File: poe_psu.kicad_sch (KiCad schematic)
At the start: 41 parts, among them T1 HR051142, U2 SI3404-A-GM, U3 EL3H7-G, U4 AN431

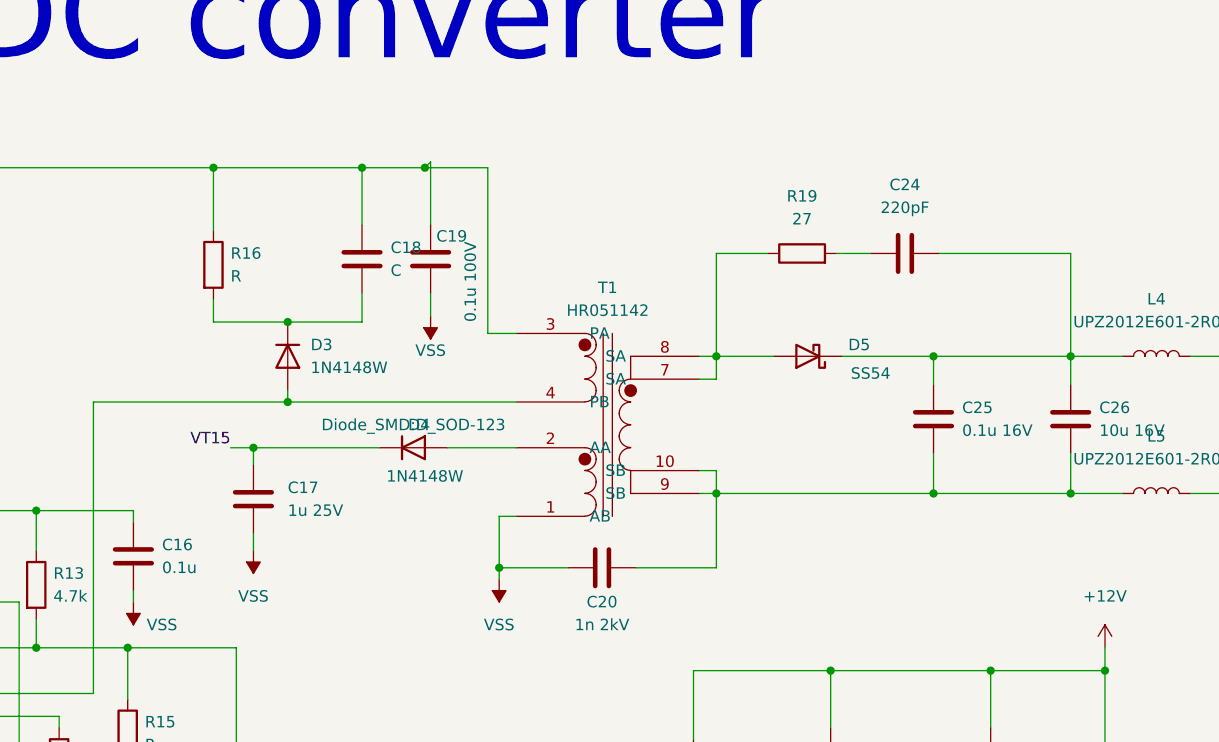
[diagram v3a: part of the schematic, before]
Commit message: Add some more footprints
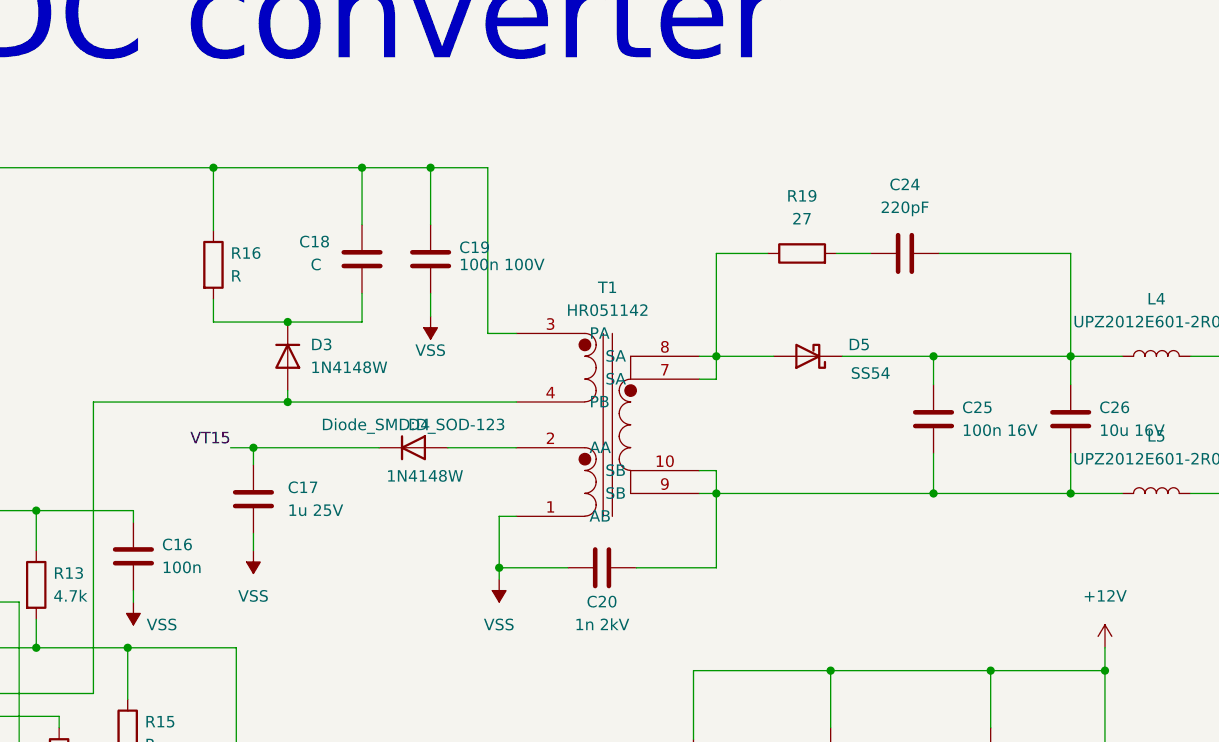
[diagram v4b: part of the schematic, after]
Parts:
- C16: value 0.1u -> 100n
- C19: value 0.1u 100V -> 100n 100V
- C21, C22, C23, C24, C26: footprint (none) -> Capacitor_SMD:C_0603_1608Metric_Pad1.08x0.95mm_HandSolder
- C25: value 0.1u 16V -> 100n 16V; footprint (none) -> Capacitor_SMD:C_0603_1608Metric_Pad1.08x0.95mm_HandSolder
- R10, R11, R12, R13, R14, R15, R16, R17, R18, R19: footprint (none) -> Resistor_SMD:R_0603_1608Metric_Pad0.98x0.95mm_HandSolder
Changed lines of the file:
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@@
   (junction (at 136.525 111.125) (diameter 0) (color 0 0 0 0)
   )
-  (junction (at 181.61 42.545) (diameter 0) (color 0 0 0 0)
-  )
   (junction (at 208.915 130.175) (diameter 0) (color 0 0 0 0)
   )
@@
   (junction (at 74.93 98.425) (diameter 0) (color 0 0 0 0)
   )
+  (junction (at 182.245 42.545) (diameter 0) (color 0 0 0 0)
+  )
   (junction (at 226.695 98.425) (diameter 0) (color 0 0 0 0)
   )
@@
     (stroke (width 0) (type default) (color 0 0 0 0))
   )
+  (wire (pts (xy 182.245 42.545) (xy 188.595 42.545))
+    (stroke (width 0) (type default) (color 0 0 0 0))
+  )
   (wire (pts (xy 138.43 80.645) (xy 130.81 80.645))
     (stroke (width 0) (type default) (color 0 0 0 0))
@@
     (stroke (width 0) (type default) (color 0 0 0 0))
   )
-  (wire (pts (xy 181.61 42.545) (xy 188.595 42.545))
+  (wire (pts (xy 174.625 42.545) (xy 182.245 42.545))
     (stroke (width 0) (type default) (color 0 0 0 0))
   )
@@
     (stroke (width 0) (type default) (color 0 0 0 0))
   )
-  (wire (pts (xy 174.625 42.545) (xy 181.61 42.545))
+  (wire (pts (xy 182.245 42.545) (xy 182.245 48.895))
     (stroke (width 0) (type default) (color 0 0 0 0))
   )
@@
     (stroke (width 0) (type default) (color 0 0 0 0))
   )
-  (wire (pts (xy 182.245 41.91) (xy 181.61 42.545))
-    (stroke (width 0) (type default) (color 0 0 0 0))
-  )
   (wire (pts (xy 211.455 98.425) (xy 226.695 98.425))
     (stroke (width 0) (type default) (color 0 0 0 0))
@@
   )
   (wire (pts (xy 130.81 100.965) (xy 144.78 100.965))
-    (stroke (width 0) (type default) (color 0 0 0 0))
-  )
-  (wire (pts (xy 182.245 41.91) (xy 182.245 48.895))
     (stroke (width 0) (type default) (color 0 0 0 0))
   )
@@
       (effects (font (size 1.27 1.27)) (justify left))
     )
-    (property "Footprint" "" (id 2) (at 254.3302 74.295 0)
+    (property "Footprint" "Capacitor_SMD:C_0603_1608Metric_Pad1.08x0.95mm_HandSolder" (id 2) (at 254.3302 74.295 0)
       (effects (font (size 1.27 1.27)) hide)
     )
@@
       (effects (font (size 1.27 1.27)) (justify left))
     )
-    (property "Value" "0.1u" (id 1) (at 152.4 86.9949 0)
+    (property "Value" "100n" (id 1) (at 152.4 86.9949 0)
       (effects (font (size 1.27 1.27)) (justify left))
     )
@@
       (effects (font (size 1.27 1.27)) (justify left))
     )
-    (property "Footprint" "" (id 2) (at 227.6602 112.395 0)
+    (property "Footprint" "Capacitor_SMD:C_0603_1608Metric_Pad1.08x0.95mm_HandSolder" (id 2) (at 227.6602 112.395 0)
       (effects (font (size 1.27 1.27)) hide)
     )
@@
     (property "Reference" "R11" (id 0) (at 81.28 90.17 90))
     (property "Value" "24.3 1%" (id 1) (at 81.28 92.075 90))
-    (property "Footprint" "" (id 2) (at 81.28 90.043 90)
+    (property "Footprint" "Resistor_SMD:R_0603_1608Metric_Pad0.98x0.95mm_HandSolder" (id 2) (at 81.28 90.043 90)
       (effects (font (size 1.27 1.27)) hide)
     )
@@
       (effects (font (size 1.27 1.27)) (justify left))
     )
-    (property "Footprint" "" (id 2) (at 245.4402 112.395 0)
+    (property "Footprint" "Capacitor_SMD:C_0603_1608Metric_Pad1.08x0.95mm_HandSolder" (id 2) (at 245.4402 112.395 0)
       (effects (font (size 1.27 1.27)) hide)
     )
@@
     (property "Reference" "C24" (id 0) (at 234.95 44.45 90))
     (property "Value" "220pF" (id 1) (at 234.95 46.99 90))
-    (property "Footprint" "" (id 2) (at 238.76 51.1048 0)
+    (property "Footprint" "Capacitor_SMD:C_0603_1608Metric_Pad1.08x0.95mm_HandSolder" (id 2) (at 238.76 51.1048 0)
       (effects (font (size 1.27 1.27)) hide)
     )
@@
     (property "Reference" "R18" (id 0) (at 228.6 123.825 90))
     (property "Value" "R" (id 1) (at 228.6 126.365 90))
-    (property "Footprint" "" (id 2) (at 228.6 131.953 90)
+    (property "Footprint" "Resistor_SMD:R_0603_1608Metric_Pad0.98x0.95mm_HandSolder" (id 2) (at 228.6 131.953 90)
       (effects (font (size 1.27 1.27)) hide)
     )
@@
     (property "Reference" "R10" (id 0) (at 81.28 80.645 90))
     (property "Value" "100K 1%" (id 1) (at 81.28 83.185 90))
-    (property "Footprint" "" (id 2) (at 81.28 87.503 90)
+    (property "Footprint" "Resistor_SMD:R_0603_1608Metric_Pad0.98x0.95mm_HandSolder" (id 2) (at 81.28 87.503 90)
       (effects (font (size 1.27 1.27)) hide)
     )
@@
   )
   (symbol (lib_id "Device:C") (at 174.625 52.705 0) (unit 1)
-    (in_bom yes) (on_board yes) (fields_autoplaced)
-    (property "Reference" "C18" (id 0) (at 177.8 51.4349 0)
-      (effects (font (size 1.27 1.27)) (justify left))
-    )
-    (property "Value" "C" (id 1) (at 177.8 53.9749 0)
+    (in_bom yes) (on_board yes)
+    (property "Reference" "C18" (id 0) (at 167.64 50.8 0)
+      (effects (font (size 1.27 1.27)) (justify left))
+    )
+    (property "Value" "C" (id 1) (at 168.91 53.34 0)
       (effects (font (size 1.27 1.27)) (justify left))
     )
@@
       (effects (font (size 1.27 1.27)) (justify left))
     )
-    (property "Footprint" "" (id 2) (at 209.677 109.855 90)
+    (property "Footprint" "Resistor_SMD:R_0603_1608Metric_Pad0.98x0.95mm_HandSolder" (id 2) (at 209.677 109.855 90)
       (effects (font (size 1.27 1.27)) hide)
     )
@@
     (property "Reference" "R12" (id 0) (at 83.185 97.79 90))
     (property "Value" "DNP" (id 1) (at 83.185 100.33 90))
-    (property "Footprint" "" (id 2) (at 83.185 105.283 90)
+    (property "Footprint" "Resistor_SMD:R_0603_1608Metric_Pad0.98x0.95mm_HandSolder" (id 2) (at 83.185 105.283 90)
       (effects (font (size 1.27 1.27)) hide)
     )
@@
       (effects (font (size 1.27 1.27)) (justify left))
     )
-    (property "Footprint" "" (id 2) (at 156.337 53.34 90)
+    (property "Footprint" "Resistor_SMD:R_0603_1608Metric_Pad0.98x0.95mm_HandSolder" (id 2) (at 156.337 53.34 90)
       (effects (font (size 1.27 1.27)) hide)
     )
@@
       (effects (font (size 1.27 1.27)) (justify left))
     )
-    (property "Value" "0.1u 16V" (id 1) (at 241.3 71.7549 0)
-      (effects (font (size 1.27 1.27)) (justify left))
-    )
-    (property "Footprint" "" (id 2) (at 239.0902 74.295 0)
+    (property "Value" "100n 16V" (id 1) (at 241.3 71.7549 0)
+      (effects (font (size 1.27 1.27)) (justify left))
+    )
+    (property "Footprint" "Capacitor_SMD:C_0603_1608Metric_Pad1.08x0.95mm_HandSolder" (id 2) (at 239.0902 74.295 0)
       (effects (font (size 1.27 1.27)) hide)
     )
@@
       (effects (font (size 1.27 1.27)) (justify left))
     )
-    (property "Footprint" "" (id 2) (at 136.652 88.9 90)
+    (property "Footprint" "Resistor_SMD:R_0603_1608Metric_Pad0.98x0.95mm_HandSolder" (id 2) (at 136.652 88.9 90)
       (effects (font (size 1.27 1.27)) hide)
     )
@@
     (property "Reference" "R19" (id 0) (at 223.52 45.72 90))
     (property "Value" "27" (id 1) (at 223.52 48.26 90))
-    (property "Footprint" "" (id 2) (at 223.52 53.848 90)
+    (property "Footprint" "Resistor_SMD:R_0603_1608Metric_Pad0.98x0.95mm_HandSolder" (id 2) (at 223.52 53.848 90)
       (effects (font (size 1.27 1.27)) hide)
     )
@@
     (property "Reference" "C21" (id 0) (at 216.535 127 90))
     (property "Value" "C" (id 1) (at 216.535 125.095 90))
-    (property "Footprint" "" (id 2) (at 220.345 129.2098 0)
+    (property "Footprint" "Capacitor_SMD:C_0603_1608Metric_Pad1.08x0.95mm_HandSolder" (id 2) (at 220.345 129.2098 0)
       (effects (font (size 1.27 1.27)) hide)
     )
@@
       (effects (font (size 1.27 1.27)) (justify left))
     )
-    (property "Footprint" "" (id 2) (at 146.812 105.41 90)
+    (property "Footprint" "Resistor_SMD:R_0603_1608Metric_Pad0.98x0.95mm_HandSolder" (id 2) (at 146.812 105.41 90)
       (effects (font (size 1.27 1.27)) hide)
     )
@@
   (symbol (lib_id "Device:C") (at 182.245 52.705 0) (unit 1)
     (in_bom yes) (on_board yes)
-    (property "Reference" "C19" (id 0) (at 182.88 50.165 0)
-      (effects (font (size 1.27 1.27)) (justify left))
-    )
-    (property "Value" "0.1u 100V" (id 1) (at 186.69 59.69 90)
+    (property "Reference" "C19" (id 0) (at 185.42 51.435 0)
+      (effects (font (size 1.27 1.27)) (justify left))
+    )
+    (property "Value" "100n 100V" (id 1) (at 185.42 53.34 0)
       (effects (font (size 1.27 1.27)) (justify left))
     )
@@
       (effects (font (size 1.27 1.27)) (justify left))
     )
-    (property "Footprint" "" (id 2) (at 139.192 108.585 90)
-      (effects (font (size 1.27 1.27)) hide)
-    )
+    (property "Footprint" "Resistor_SMD:R_0603_1608Metric_Pad0.98x0.95mm_HandSolder" (id 2) (at 139.192 108.585 90)
+      (effects (font (size 1.27 1.27)) hide)
+    )

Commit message: Add even more footprints
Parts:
- D6: footprint (none) -> Diode_SMD:D_SMA-SMB_Universal_Handsoldering
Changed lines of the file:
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@@
       (effects (font (size 1.27 1.27)) (justify right))
     )
-    (property "Footprint" "" (id 2) (at 273.05 71.12 0)
+    (property "Footprint" "Diode_SMD:D_SMA-SMB_Universal_Handsoldering" (id 2) (at 273.05 71.12 0)
       (effects (font (size 1.27 1.27)) hide)
     )

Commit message: Fixup diode footprint and add more LCSC numbers
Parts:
- C11: LCSC (none) -> C282513
- C12, C13: LCSC (none) -> C696916
- C16: LCSC (none) -> C282519
- R10: LCSC (none) -> C2906980
- R11: LCSC (none) -> C3016118
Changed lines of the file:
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@@
+      (effects (font (size 1.27 1.27)) hide)
+    )
+    (property "LCSC" "C282519" (id 4) (at 149.225 85.725 0)
       (effects (font (size 1.27 1.27)) hide)
     )
@@
       (effects (font (size 1.27 1.27)) hide)
     )
+    (property "LCSC" "C282513" (id 4) (at 31.75 92.075 0)
+      (effects (font (size 1.27 1.27)) hide)
+    )
     (pin "1")
     (pin "2")
@@
     )
     (property "Datasheet" "~" (id 3) (at 55.88 92.075 0)
+      (effects (font (size 1.27 1.27)) hide)
+    )
+    (property "LCSC" "C696916" (id 4) (at 55.88 92.075 0)
       (effects (font (size 1.27 1.27)) hide)
     )
@@
       (effects (font (size 1.27 1.27)) hide)
     )
+    (property "LCSC" "C3016118" (id 4) (at 81.28 88.265 90)
+      (effects (font (size 1.27 1.27)) hide)
+    )
     (pin "1")
     (pin "2")
@@
     )
     (property "Datasheet" "~" (id 3) (at 81.28 85.725 0)
+      (effects (font (size 1.27 1.27)) hide)
+    )
+    (property "LCSC" "C2906980" (id 4) (at 81.28 85.725 90)
       (effects (font (size 1.27 1.27)) hide)
     )
@@
       (effects (font (size 1.27 1.27)) hide)
     )
+    (property "LCSC" "C696916" (id 4) (at 80.645 67.31 0)
+      (effects (font (size 1.27 1.27)) hide)
+    )

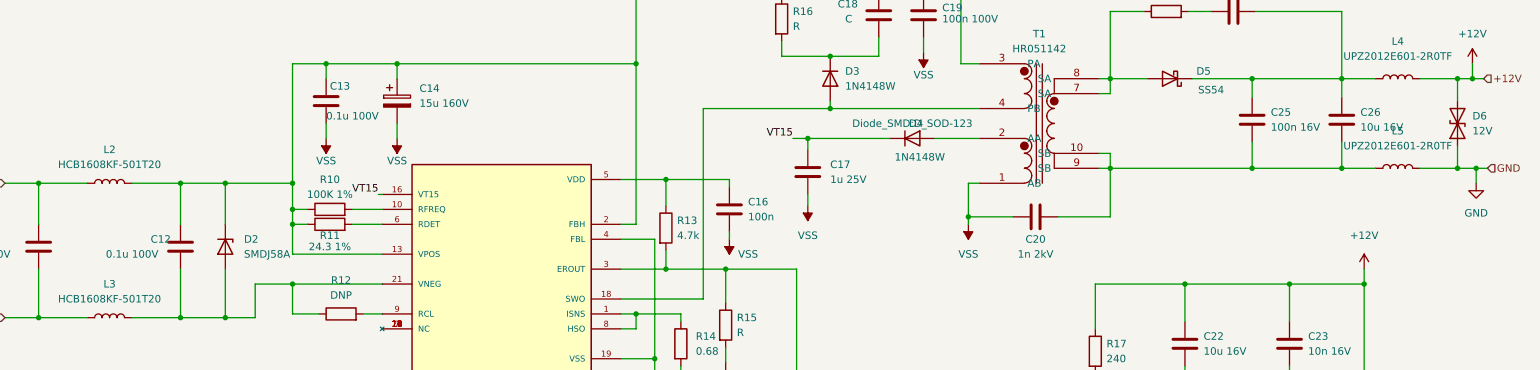
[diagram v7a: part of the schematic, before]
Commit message: Add more LCSC markings, change to electrolytic caps :
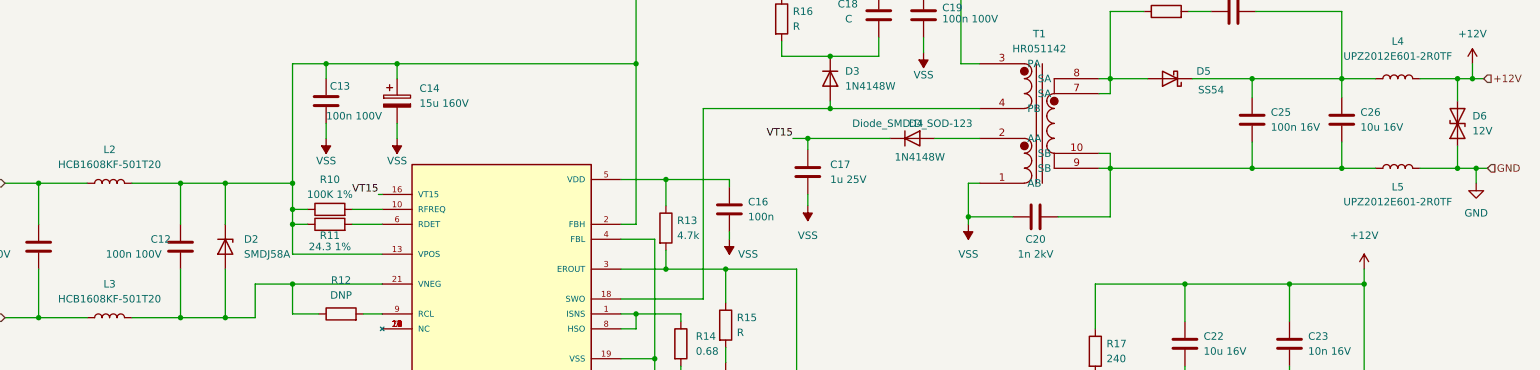
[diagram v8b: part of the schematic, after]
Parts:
- C12, C13: value 0.1u 100V -> 100n 100V
- C14: footprint Capacitor_SMD:C_0603_1608Metric_Pad1.08x0.95mm_HandSolder -> Capacitor_SMD:CP_Elec_10x10.5; LCSC (none) -> C98557
- C17: LCSC (none) -> C5673
- C19, C25: LCSC (none) -> C696916
- C22, C26: LCSC (none) -> C92487
- C23: LCSC (none) -> C163173
- C24: LCSC (none) -> C2760542
- R13: LCSC (none) -> C2907166
- R14: LCSC (none) -> C5126107
- R17: LCSC (none) -> C5140966
- R19: LCSC (none) -> C5140675
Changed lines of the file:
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@@
+      (effects (font (size 1.27 1.27)) hide)
+    )
+    (property "LCSC" "C92487" (id 4) (at 253.365 70.485 0)
       (effects (font (size 1.27 1.27)) hide)
     )
@@
       (effects (font (size 1.27 1.27)) hide)
     )
+    (property "LCSC" "C5673" (id 4) (at 162.56 79.375 0)
+      (effects (font (size 1.27 1.27)) hide)
+    )
     (pin "1")
     (pin "2")
@@
     )
     (property "Datasheet" "~" (id 3) (at 226.695 108.585 0)
+      (effects (font (size 1.27 1.27)) hide)
+    )
+    (property "LCSC" "C92487" (id 4) (at 226.695 108.585 0)
       (effects (font (size 1.27 1.27)) hide)
     )
@@
       (effects (font (size 1.27 1.27)) (justify left))
     )
-    (property "Footprint" "Capacitor_SMD:C_0603_1608Metric_Pad1.08x0.95mm_HandSolder" (id 2) (at 93.6752 71.12 0)
+    (property "Footprint" "Capacitor_SMD:CP_Elec_10x10.5" (id 2) (at 93.6752 71.12 0)
       (effects (font (size 1.27 1.27)) hide)
     )
     (property "Datasheet" "~" (id 3) (at 92.71 67.31 0)
+      (effects (font (size 1.27 1.27)) hide)
+    )
+    (property "LCSC" "C98557" (id 4) (at 92.71 67.31 0)
       (effects (font (size 1.27 1.27)) hide)
     )
@@
       (effects (font (size 1.27 1.27)) (justify left))
     )
-    (property "Value" "0.1u 100V" (id 1) (at 43.18 93.345 0)
+    (property "Value" "100n 100V" (id 1) (at 43.18 93.345 0)
       (effects (font (size 1.27 1.27)) (justify left))
     )
@@
       (effects (font (size 1.27 1.27)) hide)
     )
+    (property "LCSC" "C163173" (id 4) (at 244.475 108.585 0)
+      (effects (font (size 1.27 1.27)) hide)
+    )
     (pin "1")
     (pin "2")
@@
     )
     (property "Datasheet" "~" (id 3) (at 234.95 52.07 0)
+      (effects (font (size 1.27 1.27)) hide)
+    )
+    (property "LCSC" "C2760542" (id 4) (at 234.95 52.07 90)
       (effects (font (size 1.27 1.27)) hide)
     )
@@
       (effects (font (size 1.27 1.27)) hide)
     )
+    (property "LCSC" "C5140966" (id 4) (at 211.455 109.855 0)
+      (effects (font (size 1.27 1.27)) hide)
+    )
     (pin "1")
     (pin "2")
@@
       (effects (font (size 1.27 1.27)) (justify left))
     )
-    (property "Value" "0.1u 100V" (id 1) (at 80.645 69.85 0)
+    (property "Value" "100n 100V" (id 1) (at 80.645 69.85 0)
       (effects (font (size 1.27 1.27)) (justify left))
     )
@@
       (effects (font (size 1.27 1.27)) hide)
     )
+    (property "LCSC" "C696916" (id 4) (at 238.125 70.485 0)
+      (effects (font (size 1.27 1.27)) hide)
+    )
     (pin "1")
     (pin "2")
@@
     )
     (property "Datasheet" "~" (id 3) (at 138.43 88.9 0)
+      (effects (font (size 1.27 1.27)) hide)
+    )
+    (property "LCSC" "C2907166" (id 4) (at 138.43 88.9 0)
       (effects (font (size 1.27 1.27)) hide)
     )
@@
   )
   (symbol (lib_id "Device:L") (at 262.89 78.74 90) (unit 1)
-    (in_bom yes) (on_board yes) (fields_autoplaced)
-    (property "Reference" "L5" (id 0) (at 262.89 72.39 90))
-    (property "Value" "UPZ2012E601-2R0TF" (id 1) (at 262.89 74.93 90))
+    (in_bom yes) (on_board yes)
+    (property "Reference" "L5" (id 0) (at 262.89 81.915 90))
+    (property "Value" "UPZ2012E601-2R0TF" (id 1) (at 262.89 84.455 90))
     (property "Footprint" "Inductor_SMD:L_0805_2012Metric_Pad1.15x1.40mm_HandSolder" (id 2) (at 262.89 78.74 0)
       (effects (font (size 1.27 1.27)) hide)
@@
       (effects (font (size 1.27 1.27)) hide)
     )
+    (property "LCSC" "C5140675" (id 4) (at 223.52 52.07 90)
+      (effects (font (size 1.27 1.27)) hide)
+    )
     (pin "1")
     (pin "2")
@@
       (effects (font (size 1.27 1.27)) hide)
     )
+    (property "LCSC" "C696916" (id 4) (at 182.245 52.705 0)
+      (effects (font (size 1.27 1.27)) hide)
+    )
     (pin "1")
     (pin "2")
@@
       (effects (font (size 1.27 1.27)) hide)
     )
+    (property "LCSC" "C5126107" (id 4) (at 140.97 108.585 0)
+      (effects (font (size 1.27 1.27)) hide)
+    )
